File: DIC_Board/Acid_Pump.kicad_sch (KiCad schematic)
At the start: 0 parts

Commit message: Completed Acid Pump sheet
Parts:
- added C320: 2.2uF 16V, Capacitor_SMD:C_0603_1608Metric, symbol Device:C
- added C321: 22uF 16V, Capacitor_SMD:C_1210_3225Metric, symbol Device:C
- added C322: 10nF, Capacitor_SMD:C_0603_1608Metric, symbol Device:C
- added C323: 1nF, Capacitor_SMD:C_0603_1608Metric, symbol Device:C
- added C324: 22nF, Capacitor_SMD:C_0603_1608Metric, symbol Device:C
- added J32: 0430450400, Connector_Molex:Molex_Micro-Fit_3.0_43045-0400_2x02_P3.00mm_Horizontal, symbol Connector_Generic:Conn_02x02_Odd_Even
- added R320, R321: 0.5R 1W, Resistor_SMD:R_1206_3216Metric, symbol Device:R
- added R322, R323: 18k, Resistor_SMD:R_0603_1608Metric, symbol Device:R
- added R324, R325: 20k, Resistor_SMD:R_0603_1608Metric, symbol Device:R
- added R326: 47k, Resistor_SMD:R_0603_1608Metric, symbol Device:R
- added R327: 1k, Resistor_SMD:R_0603_1608Metric, symbol Device:R
- added R328: 60k, Resistor_SMD:R_0603_1608Metric, symbol Device:R
- added R329: 1.87k, Resistor_SMD:R_0603_1608Metric, symbol Device:R
- added U32: STSPIN220, Package_DFN_QFN:VQFN-16-1EP_3x3mm_P0.5mm_EP1.8x1.8mm, symbol Driver_Motor:STSPIN220
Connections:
- new net: J32.3 (Pin_3), U32.10 (OUTB1)
- new net: R328.2, R329.1, U32.11 (REF)
- new net: R326.1, R327.1, U32.12 (TOFF)
- new net: J32.1 (Pin_1), U32.3 (OUTA1)
- new net: R320.1, U32.4 (SENSEA)
- new net: J32.2 (Pin_2), U32.5 (OUTA2)
- new net: J32.4 (Pin_4), U32.8 (OUTB2)
- new net: R321.1, U32.9 (SENSEB)
- new net: C324.1, R327.2
- new net +2V8: C320.1, C321.1, U32.6 (VS)
- new net +3V3: R322.1, R323.1, R324.1, R328.1, U32.15 (MODE2)
- new net ACID_PUMP_DIR: R324.2, U32.1 (DIR)
- new net ACID_PUMP_EN_FAULT_N: C322.1, R322.2, U32.13 (EN/FLT)
- new net ACID_PUMP_RESET_N: C323.1, R323.2, U32.14 (STBY/RESET)
- new net ACID_PUMP_STEP: R325.1, U32.2 (STCK)
- new net GND: C320.2, C321.2, C322.2, C323.2, C324.2, R320.2, R321.2, R325.2, R326.2, R329.2, U32.16 (MODE1), U32.17 (EPAD), U32.7 (GND)
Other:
- note added: "ACID PUMP STEPPER DRIVER — STSPIN220, +2V8 MOTOR SUPPLY"
- note added: "Current limit: 0.5 ohm sense, VREF adjustable 0–0.471 V; IPEAK approximately VREF/RSENSE = 0–0.94 A."
- note added: "Firmware must preserve STEP low and DIR high while releasing RESET; afterwards they are normal controls."
- note added: "Fixed 1/4-step latch: MODE1=0, MODE2=1, STEP=0 and DIR=1 when STBY/RESET rises."
- note added: "Place C320/C321 and both sense resistors close to U32. EPAD requires solid GND and thermal vias."

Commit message: Checkpoint current schematic state
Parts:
- removed J32: 0430450400, Connector_Molex:Molex_Micro-Fit_3.0_43045-0400_2x02_P3.00mm_Horizontal, symbol Connector_Generic:Conn_02x02_Odd_Even
- added J9: Conn_01x04, symbol Connector_Generic:Conn_01x04
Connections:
- net at U32.10 (OUTB1): now also J9.3 (Pin_3)
- net at U32.3 (OUTA1): now also J9.1 (Pin_1)
- net at U32.5 (OUTA2): now also J9.2 (Pin_2)
- net at U32.8 (OUTB2): now also J9.4 (Pin_4)
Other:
- moved on the sheet: R322, R323, R324, R325

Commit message: Synchronize schematic hierarchy and MCU pin map
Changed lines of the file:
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@@
-		)
-	)
-	(global_label "ACID_PUMP_RESET_N"
-		(shape input)
-		(at 48.26 115.57 180)
-		(fields_autoplaced yes)
-		(effects
-			(font
-				(size 1.27 1.27)
-			)
-			(justify right)
-		)
-		(property "Intersheetrefs" "${INTERSHEET_REFS}"
-			(at 48.26 115.57 0)
-			(hide yes)
-			(show_name no)
-			(do_not_autoplace no)
-			(effects
-				(font
-					(size 1.27 1.27)
-				)
-			)
 		)
 	)
@@
 		)
 	)
-	(global_label "ACID_PUMP_EN_FAULT_N"
-		(shape bidirectional)
-		(at 49.53 101.6 180)
-		(fields_autoplaced yes)
+	(hierarchical_label "ACID_PUMP_RESET_N"
+		(shape input)
+		(at 48.26 115.57 180)
 		(effects
 			(font
@@
 			(justify right)
 		)
-		(property "Intersheetrefs" "${INTERSHEET_REFS}"
-			(at 49.53 101.6 0)
-			(hide yes)
-			(show_name no)
-			(do_not_autoplace no)
-			(effects
-				(font
-					(size 1.27 1.27)
-				)
-			)
-		)
 	)
-	(global_label "ACID_PUMP_STEP"
-		(shape input)
-		(at 49.53 88.9 180)
-		(fields_autoplaced yes)
+	(hierarchical_label "ACID_PUMP_EN_FAULT_N"
+		(shape bidirectional)
+		(at 49.53 101.6 180)
 		(effects
 			(font
@@
 			(justify right)
 		)
-		(property "Intersheetrefs" "${INTERSHEET_REFS}"
-			(at 49.53 88.9 0)
-			(hide yes)
-			(show_name no)
-			(do_not_autoplace no)
-			(effects
-				(font
-					(size 1.27 1.27)
-				)
-			)
-		)
 	)
-	(global_label "ACID_PUMP_DIR"
+	(hierarchical_label "ACID_PUMP_STEP"
 		(shape input)
-		(at 49.53 86.36 180)
-		(fields_autoplaced yes)
+		(at 49.53 88.9 180)
 		(effects
 			(font
@@
 			(justify right)
 		)
-		(property "Intersheetrefs" "${INTERSHEET_REFS}"
-			(at 31.9095 86.36 0)
-			(hide yes)
-			(show_name no)
-			(do_not_autoplace no)
-			(effects
-				(font
-					(size 1.27 1.27)
-				)
-				(justify right)
+	)
+	(hierarchical_label "ACID_PUMP_DIR"
+		(shape input)
+		(at 49.53 86.36 180)
+		(effects
+			(font
+				(size 1.27 1.27)
 			)
+			(justify right)
 		)
 	)

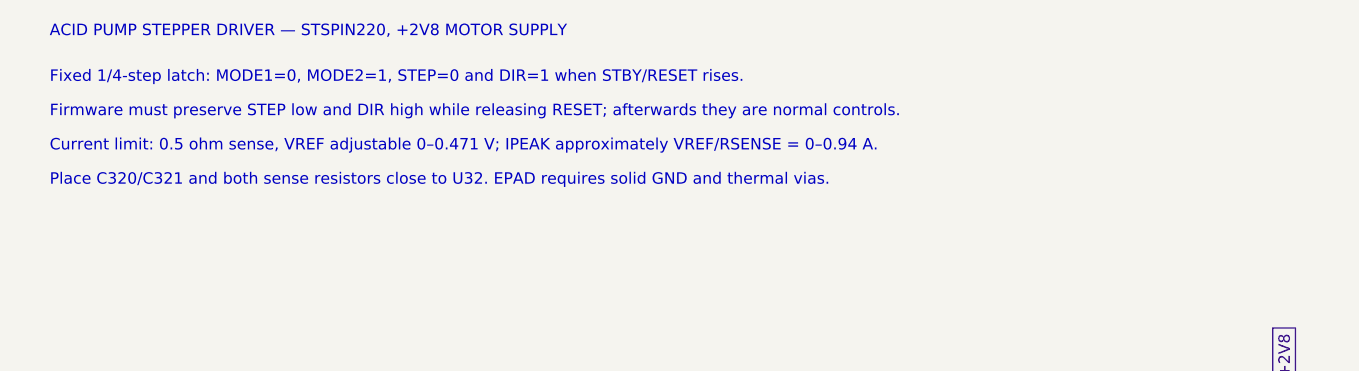
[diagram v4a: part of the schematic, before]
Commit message: Synchronize power, communications, and MCU configuration
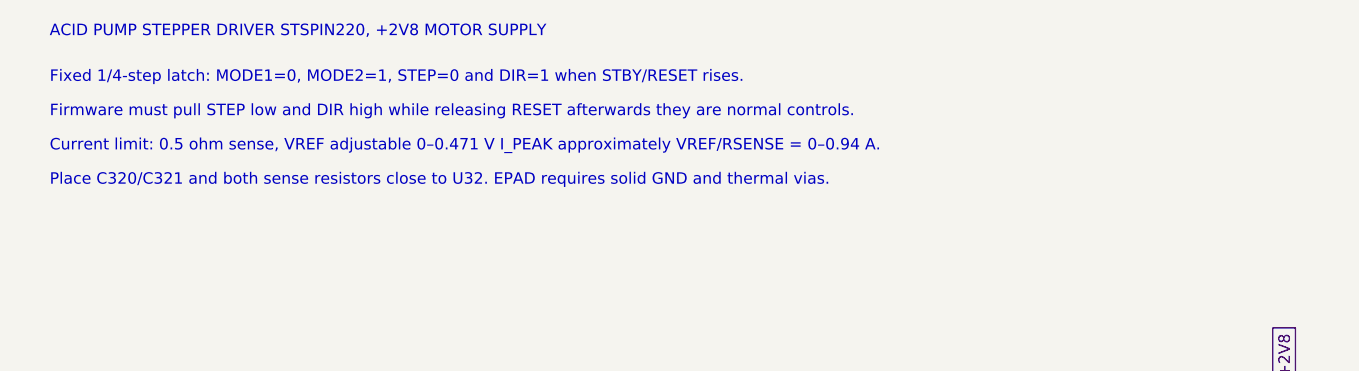
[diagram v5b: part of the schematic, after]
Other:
- note added: "ACID PUMP STEPPER DRIVER STSPIN220, +2V8 MOTOR SUPPLY"
- note added: "Current limit: 0.5 ohm sense, VREF adjustable 0–0.471 V I_PEAK approximately VREF/RSENSE = 0–0.94 A."
- note added: "Firmware must pull STEP low and DIR high while releasing RESET afterwards they are normal controls."
- note removed: "ACID PUMP STEPPER DRIVER — STSPIN220, +2V8 MOTOR SUPPLY"
- note removed: "Current limit: 0.5 ohm sense, VREF adjustable 0–0.471 V; IPEAK approximately VREF/RSENSE = 0–0.94 A."
- note removed: "Firmware must preserve STEP low and DIR high while releasing RESET; afterwards they are normal controls."
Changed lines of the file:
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@@
 		(comment 2 "+2V8 motor supply; adjustable 0–0.94 A peak current limit")
 	)
-	(text "Firmware must preserve STEP low and DIR high while releasing RESET; afterwards they are normal controls."
+	(text "Firmware must pull STEP low and DIR high while releasing RESET afterwards they are normal controls."
 		(exclude_from_sim no)
 		(at 25.4 29.21 0)
@@
 		)
 	)
-	(text "ACID PUMP STEPPER DRIVER — STSPIN220, +2V8 MOTOR SUPPLY"
+	(text "ACID PUMP STEPPER DRIVER STSPIN220, +2V8 MOTOR SUPPLY"
 		(exclude_from_sim no)
 		(at 25.4 20.32 0)
@@
 		)
 	)
-	(text "Current limit: 0.5 ohm sense, VREF adjustable 0–0.471 V; IPEAK approximately VREF/RSENSE = 0–0.94 A."
+	(text "Current limit: 0.5 ohm sense, VREF adjustable 0–0.471 V I_PEAK approximately VREF/RSENSE = 0–0.94 A."
 		(exclude_from_sim no)
 		(at 25.4 33.02 0)

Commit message: Pump fixes + doc extraction
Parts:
- added RV1: 10k trim, Potentiometer_SMD:Potentiometer_Bourns_3314J_Vertical, symbol Device:R_Potentiometer_Trim
- R320, R321: value 0.5R 1W -> 2.00R 1%
- R328: value 60k -> 2.87k
- R329: value 1.87k -> 482R
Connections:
- net at R329.1, U32.11 (REF): now also RV1.2, RV1.3; no longer R328.2
- new net: R328.2, RV1.1
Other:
- note added: "Current limit: 2.00 ohm sense; RV1 adjusts ~0.06-0.24 A nominal. Set VREF=0.218 V (~4.0k trim) for I_PEAK~0.109 A."
- note added: "Design basis: ~0.11 A provides margin over the Aquatech BD202411-T 0.1 A output. Validate the installed RP-TX winding and ramp STEP rate."
- note added: "Tie RV1 wiper to its VREF-side terminal. Use >=0.25 W sense resistors; place them and C320/C321 close to U32."
- note removed: "Current limit: 0.5 ohm sense, VREF adjustable 0–0.471 V I_PEAK approximately VREF/RSENSE = 0–0.94 A."
- note removed: "Place C320/C321 and both sense resistors close to U32. EPAD requires solid GND and thermal vias."
- moved on the sheet: C322, R322, R328, R329

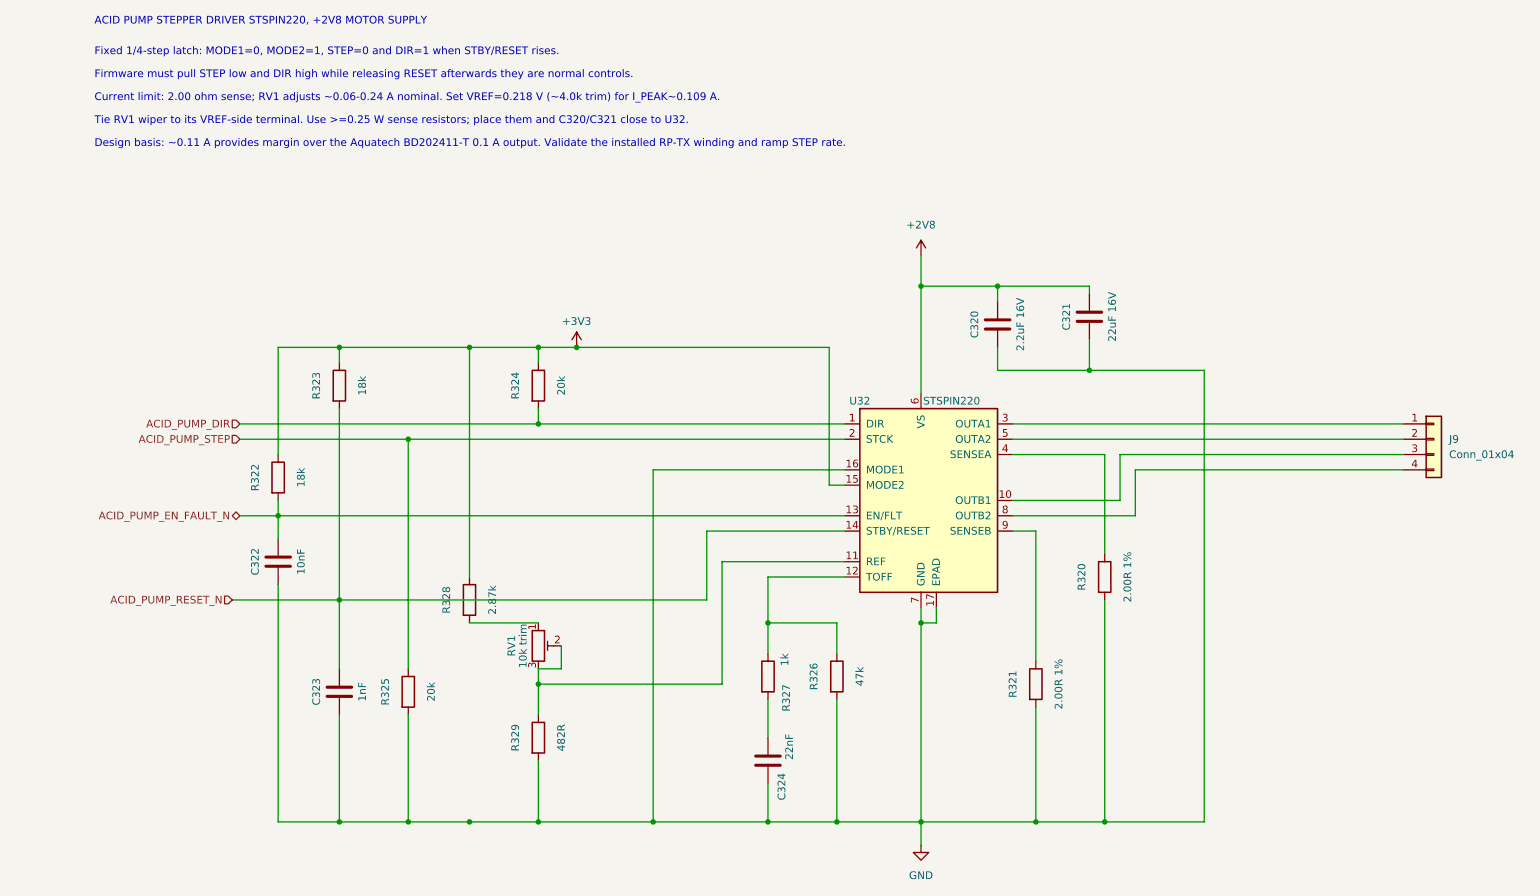
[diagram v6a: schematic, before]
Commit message: Updated board for layout! All footprints added
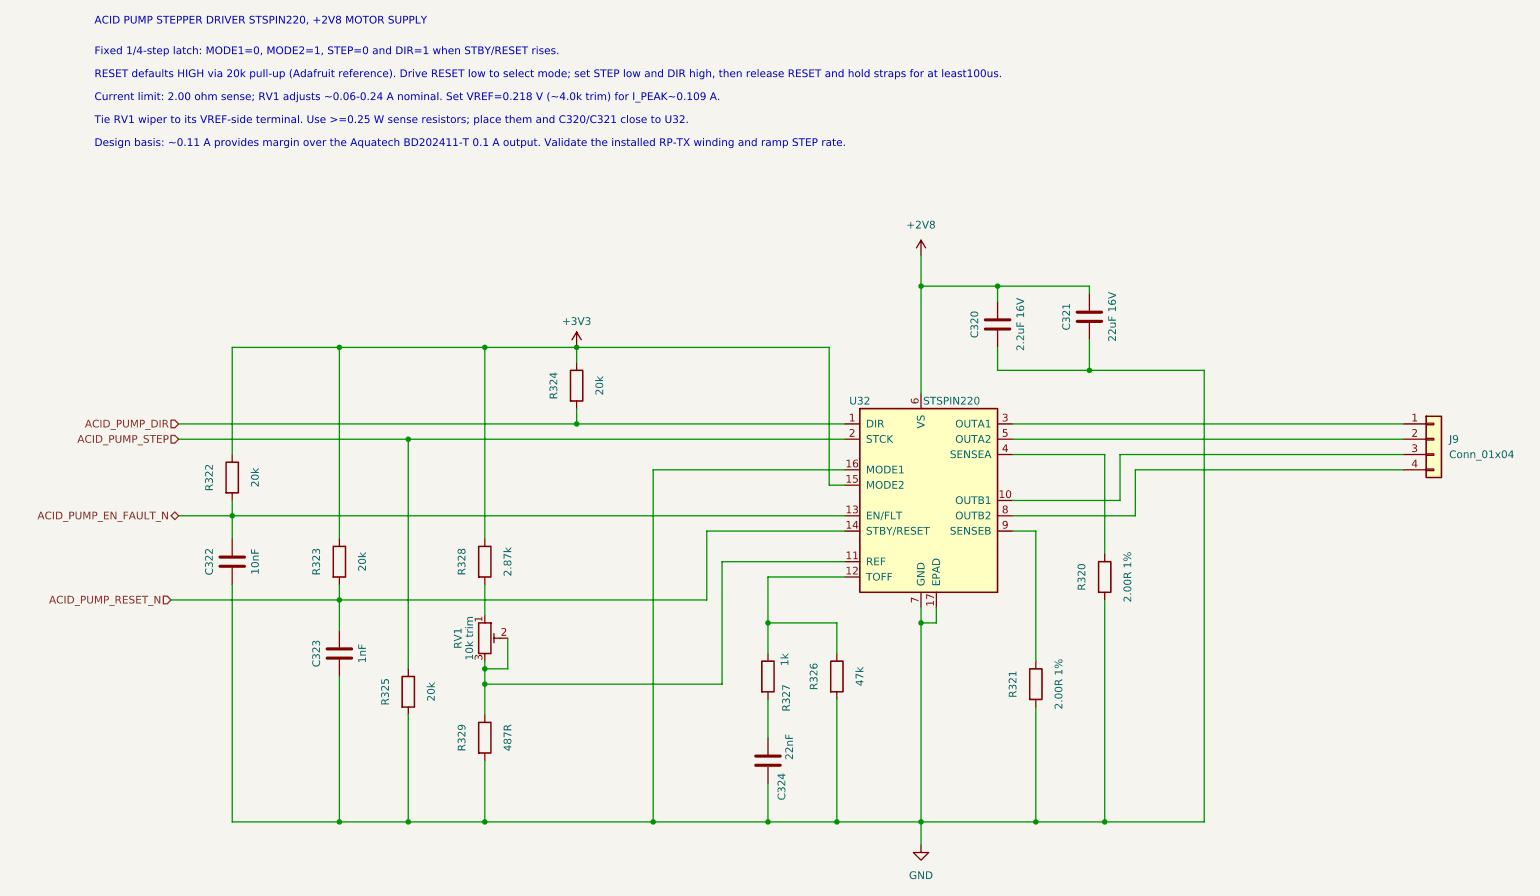
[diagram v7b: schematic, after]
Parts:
- C320: BOM Source (none) -> https://product.tdk.com/en/search/capacitor/ceramic/mlcc/in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; Dielectric (none) -> X5R; MPN (none) -> C1608X5R1C225K080AB; Manufacturer (none) -> TDK; Tolerance (none) -> 10%; Voltage Rating (none) -> 16V
- C321: BOM Source (none) -> https://www.murata.com/en-us/products/productdetail.aspx?pa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; Dielectric (none) -> X7R; MPN (none) -> GRM32ER71E226ME15L; Manufacturer (none) -> Murata; Tolerance (none) -> 20%; Voltage Rating (none) -> 25V
- C322: BOM Source (none) -> https://product.tdk.com/en/search/capacitor/ceramic/mlcc/in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; Dielectric (none) -> X7R; MPN (none) -> C1608X7R1H103K080AA; Manufacturer (none) -> TDK; Tolerance (none) -> 10%; Voltage Rating (none) -> 50V
- C323: BOM Source (none) -> https://product.tdk.com/en/search/capacitor/ceramic/mlcc/in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; Dielectric (none) -> C0G; MPN (none) -> C1608C0G1H102J080AA; Manufacturer (none) -> TDK; Tolerance (none) -> 5%; Voltage Rating (none) -> 50V
- C324: BOM Source (none) -> https://product.tdk.com/en/search/capacitor/ceramic/mlcc/in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; Dielectric (none) -> X7R; MPN (none) -> C1608X7R1H223K080AA; Manufacturer (none) -> TDK; Tolerance (none) -> 10%; Voltage Rating (none) -> 50V
- J9: footprint (none) -> Connector_Molex:Molex_Micro-Fit_3.0_43045-0400_2x02_P3.00mm_Horizontal; BOM Source (none) -> https://www.molex.com/en-us/products/part-detail/430450400; MPN (none) -> 0430450400; Manufacturer (none) -> Molex
- R320, R321: BOM Source (none) -> https://www.vishay.com/docs/20035/dcrcwe3.pdf; MPN (none) -> CRCW12062R00FKEA; Manufacturer (none) -> Vishay; Power Rating (none) -> 0.25W; Tolerance (none) -> 1%
- R322, R323: value 18k -> 20k; BOM Source (none) -> https://www.vishay.com/docs/20035/dcrcwe3.pdf; MPN (none) -> CRCW060320K0FKEA; Manufacturer (none) -> Vishay; Power Rating (none) -> 0.125W; Tolerance (none) -> 1%
- R324, R325: BOM Source (none) -> https://www.vishay.com/docs/20035/dcrcwe3.pdf; MPN (none) -> CRCW060320K0FKEA; Manufacturer (none) -> Vishay; Power Rating (none) -> 0.125W; Tolerance (none) -> 1%
- R326: BOM Source (none) -> https://www.vishay.com/docs/20035/dcrcwe3.pdf; MPN (none) -> CRCW060347K0FKEA; Manufacturer (none) -> Vishay; Power Rating (none) -> 0.125W; Tolerance (none) -> 1%
- R327: BOM Source (none) -> https://www.vishay.com/docs/20035/dcrcwe3.pdf; MPN (none) -> CRCW06031K00FKEA; Manufacturer (none) -> Vishay; Power Rating (none) -> 0.125W; Tolerance (none) -> 1%
- R328: BOM Source (none) -> https://www.vishay.com/docs/28758/tnpw_e3.pdf; MPN (none) -> TNPW06032K87BEEA; Manufacturer (none) -> Vishay; Power Rating (none) -> 0.125W; TCR (none) -> 25ppm/K; Tolerance (none) -> 0.1%
- R329: value 482R -> 487R; BOM Source (none) -> https://www.vishay.com/docs/28758/tnpw_e3.pdf; MPN (none) -> TNPW0603487RBEEA; Manufacturer (none) -> Vishay; Power Rating (none) -> 0.125W; TCR (none) -> 25ppm/K; Tolerance (none) -> 0.1%
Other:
- note added: "RESET defaults HIGH via 20k pull-up (Adafruit reference). Drive RESET low to select mode; set STEP low and DIR high, then release RESET and hold straps for at least100us."
- note removed: "Firmware must pull STEP low and DIR high while releasing RESET afterwards they are normal controls."
- moved on the sheet: C322, C323, R323, R324, R328, R329, RV1
